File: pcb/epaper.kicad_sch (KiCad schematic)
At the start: 20 parts, among them J1 Conn_01x24, Q1 Si1308EDL

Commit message: pcb: rev 2?
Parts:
- J1: footprint (none) -> live-caption-badge:FPC05024-13200_1x24-1MP_P0.50_Horizontal
- L1: footprint (none) -> live-caption-badge:L_Bourns-SDEE0406A
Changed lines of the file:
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@@
 			)
 		)
-		(property "Footprint" ""
+		(property "Footprint" "live-caption-badge:L_Bourns-SDEE0406A"
 			(at 147.32 76.2 0)
 			(effects
@@
 			)
 		)
-		(property "Footprint" ""
+		(property "Footprint" "live-caption-badge:FPC05024-13200_1x24-1MP_P0.50_Horizontal"
 			(at 100.33 66.04 0)
 			(effects

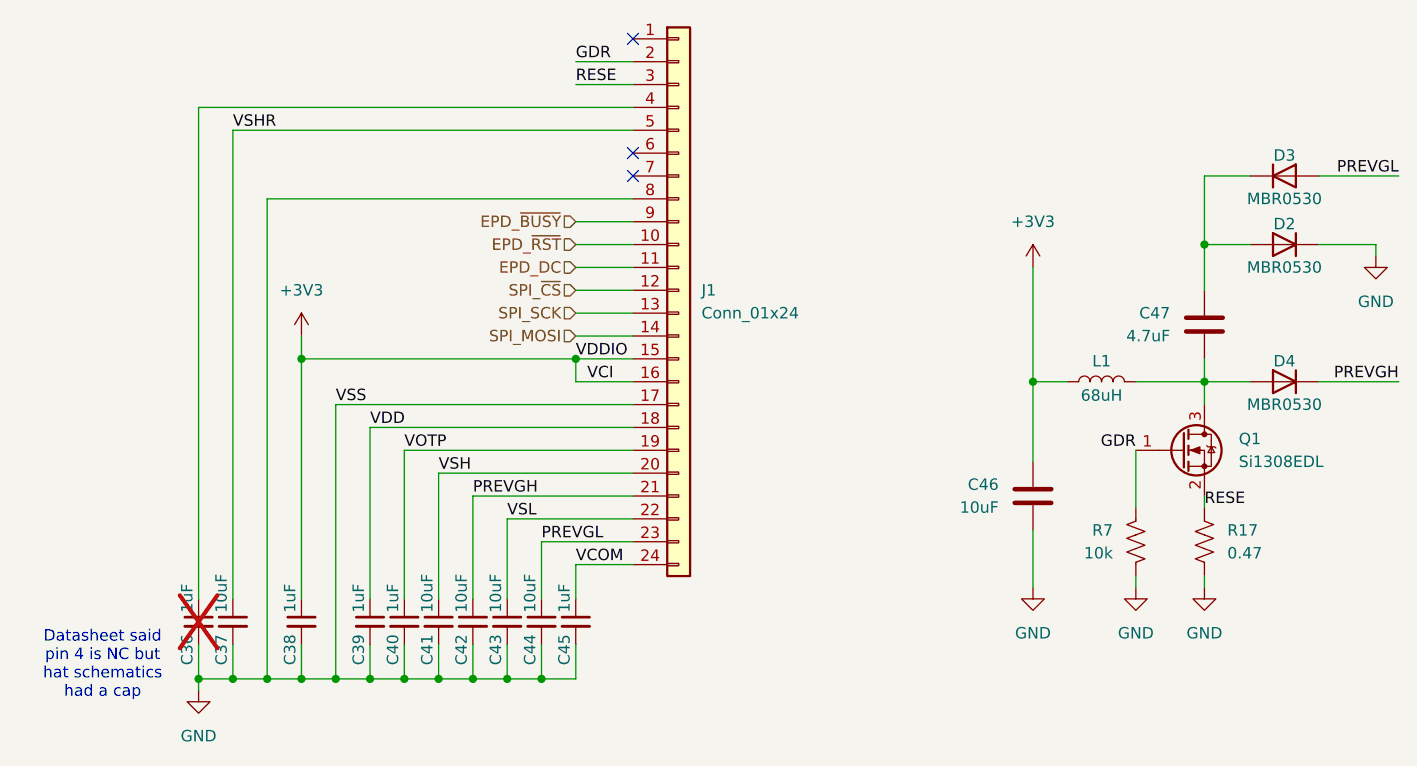
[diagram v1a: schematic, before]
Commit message: pcb: Flip FPC, 170x105mm
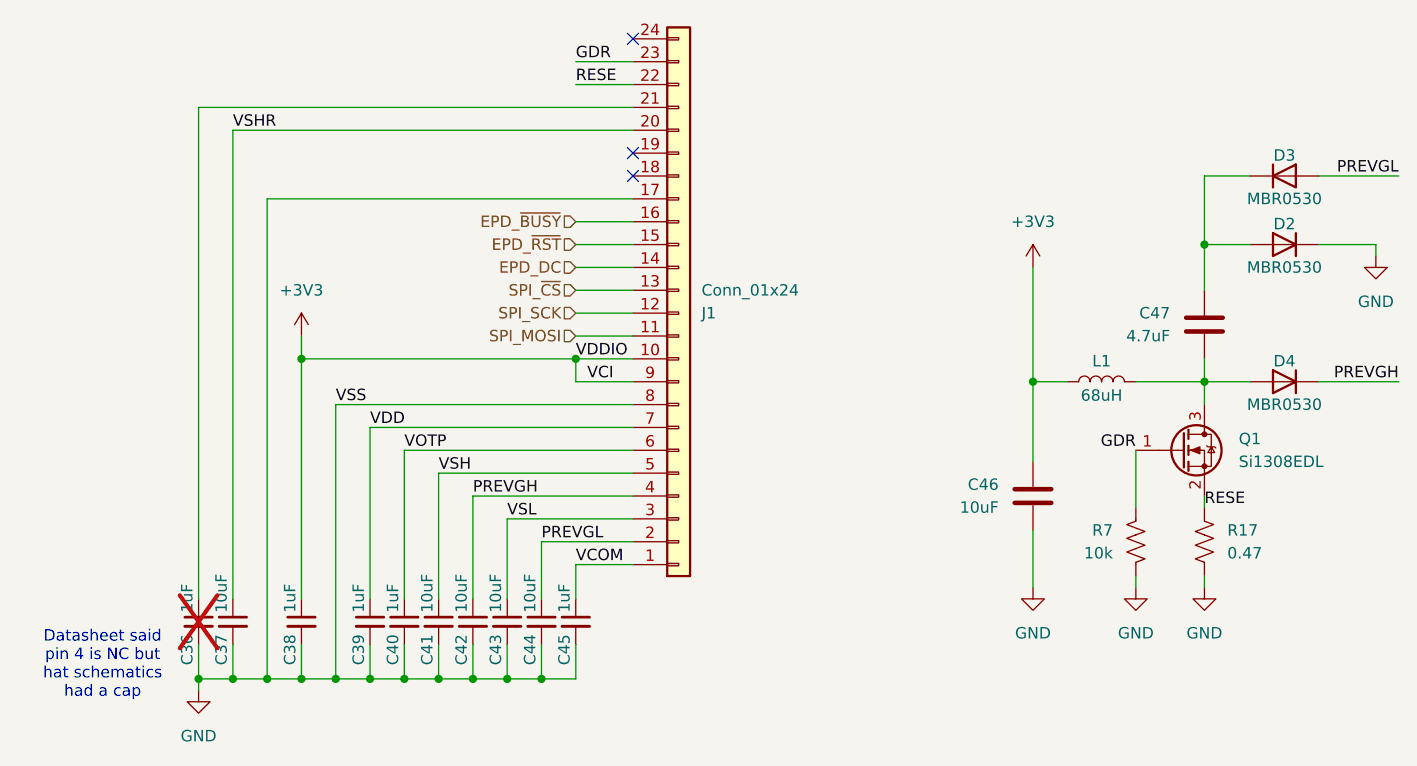
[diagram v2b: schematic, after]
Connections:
- net +3V3: now also J1.10 (Pin_10), J1.9 (Pin_9); no longer J1.15 (Pin_15), J1.16 (Pin_16)
- net EPD_DC: now also J1.14 (Pin_14); no longer J1.11 (Pin_11)
- net EPD_~{BUSY}: now also J1.16 (Pin_16); no longer J1.9 (Pin_9)
- net EPD_~{RST}: now also J1.15 (Pin_15); no longer J1.10 (Pin_10)
- net GDR: now also J1.23 (Pin_23); no longer J1.2 (Pin_2)
- net PREVGH: now also J1.4 (Pin_4); no longer J1.21 (Pin_21)
- net PREVGL: now also J1.2 (Pin_2); no longer J1.23 (Pin_23)
- net RESE: now also J1.22 (Pin_22); no longer J1.3 (Pin_3)
- net SPI_MOSI: now also J1.11 (Pin_11); no longer J1.14 (Pin_14)
- net SPI_SCK: now also J1.12 (Pin_12); no longer J1.13 (Pin_13)
- net SPI_~{CS}: now also J1.13 (Pin_13); no longer J1.12 (Pin_12)
- net VCOM: now also J1.1 (Pin_1); no longer J1.24 (Pin_24)
- net VDD: now also J1.7 (Pin_7); no longer J1.18 (Pin_18)
- net VOTP: now also J1.6 (Pin_6); no longer J1.19 (Pin_19)
- net VSH: now also J1.5 (Pin_5); no longer J1.20 (Pin_20)
- net VSHR: now also J1.20 (Pin_20); no longer J1.5 (Pin_5)
- net VSL: now also J1.3 (Pin_3); no longer J1.22 (Pin_22)
- net at C36.1: now also J1.21 (Pin_21); no longer J1.4 (Pin_4)
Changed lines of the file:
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@@
 	(symbol
 		(lib_id "Connector_Generic:Conn_01x24")
-		(at 100.33 66.04 0)
+		(at 100.33 68.58 0)
+		(mirror x)
 		(unit 1)
 		(exclude_from_sim no)
@@
 		(on_board yes)
 		(dnp no)
-		(fields_autoplaced yes)
 		(property "Reference" "J1"
-			(at 102.87 66.0399 0)
+			(at 102.87 68.5801 0)
 			(effects
 				(font
@@
 		)
 		(property "Value" "Conn_01x24"
-			(at 102.87 68.5799 0)
+			(at 102.87 66.0401 0)
 			(effects
 				(font
@@
 		)
 		(property "Footprint" "live-caption-badge:FPC05024-13200_1x24-1MP_P0.50_Horizontal"
-			(at 100.33 66.04 0)
+			(at 100.33 68.58 0)
 			(effects
 				(font
@@
 		)
 		(property "Datasheet" "~"
-			(at 100.33 66.04 0)
+			(at 100.33 68.58 0)
 			(effects
 				(font
@@
 		)
 		(property "Description" "Generic connector, single row, 01x24, script generated (kicad-library-utils/schlib/autogen/connector/)"
-			(at 100.33 66.04 0)
+			(at 100.33 68.58 0)
 			(effects
 				(font

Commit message: pcb: rev 2 ready?
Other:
- note added: "Insert ribbon cable <-- this way"
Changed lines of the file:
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@@
+		)
+	)
+	(text "Insert ribbon cable\n<-- this way"
+		(exclude_from_sim no)
+		(at 103.378 61.976 0)
+		(effects
+			(font
+				(size 1.27 1.27)
+			)
+			(justify left)
 		)
 	)

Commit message: pcb: Change paper size to US Letter
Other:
- title: E-Paper -> Live Caption Badge - E-Paper Subsystem
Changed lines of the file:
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@@
 	(generator "eeschema")
 	(generator_version "8.0")
-	(paper "A4")
+	(paper "USLetter")
 	(title_block
-		(title "E-Paper")
+		(title "Live Caption Badge - E-Paper Subsystem")
 		(date "2024-11-21")
 		(rev "2")
